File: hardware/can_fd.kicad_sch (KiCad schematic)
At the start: 11 parts

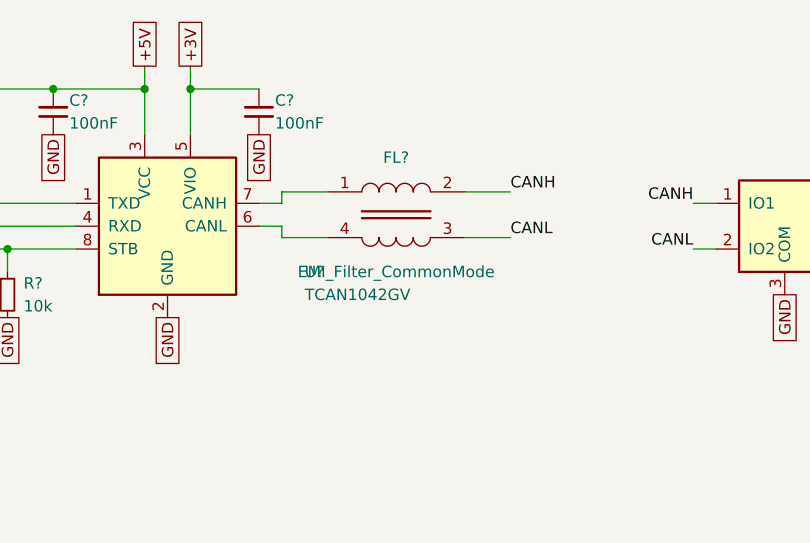
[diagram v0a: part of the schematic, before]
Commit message: Add sensing sheet; update MCU, CAN FD, encoder and root schematics
Co-Authored-By: Claude Opus 5.5 <noreply@anthropic.com>
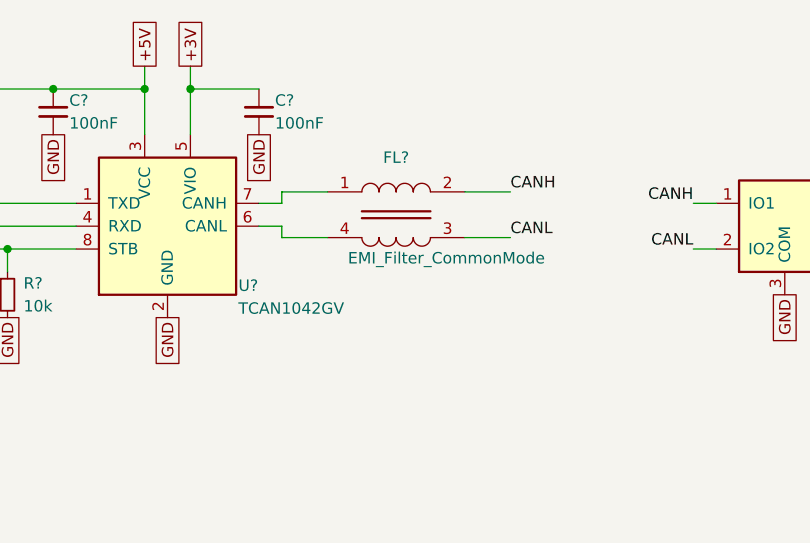
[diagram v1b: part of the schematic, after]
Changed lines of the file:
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@@
 		)
 		(property "Value" "EMI_Filter_CommonMode"
-			(at 127 106.68 0)
+			(at 132.588 105.156 0)
 			(show_name no)
 			(do_not_autoplace no)
@@
 		(dnp no)
 		(property "Reference" "U?"
-			(at 116.84 106.68 0)
+			(at 109.474 108.204 0)
 			(show_name no)
 			(do_not_autoplace no)
@@
 		)
 		(property "Value" "TCAN1042GV"
-			(at 116.84 109.22 0)
-			(show_name no)
-			(do_not_autoplace no)
+			(at 109.474 110.744 0)
+			(show_name no)
+			(do_not_autoplace no)

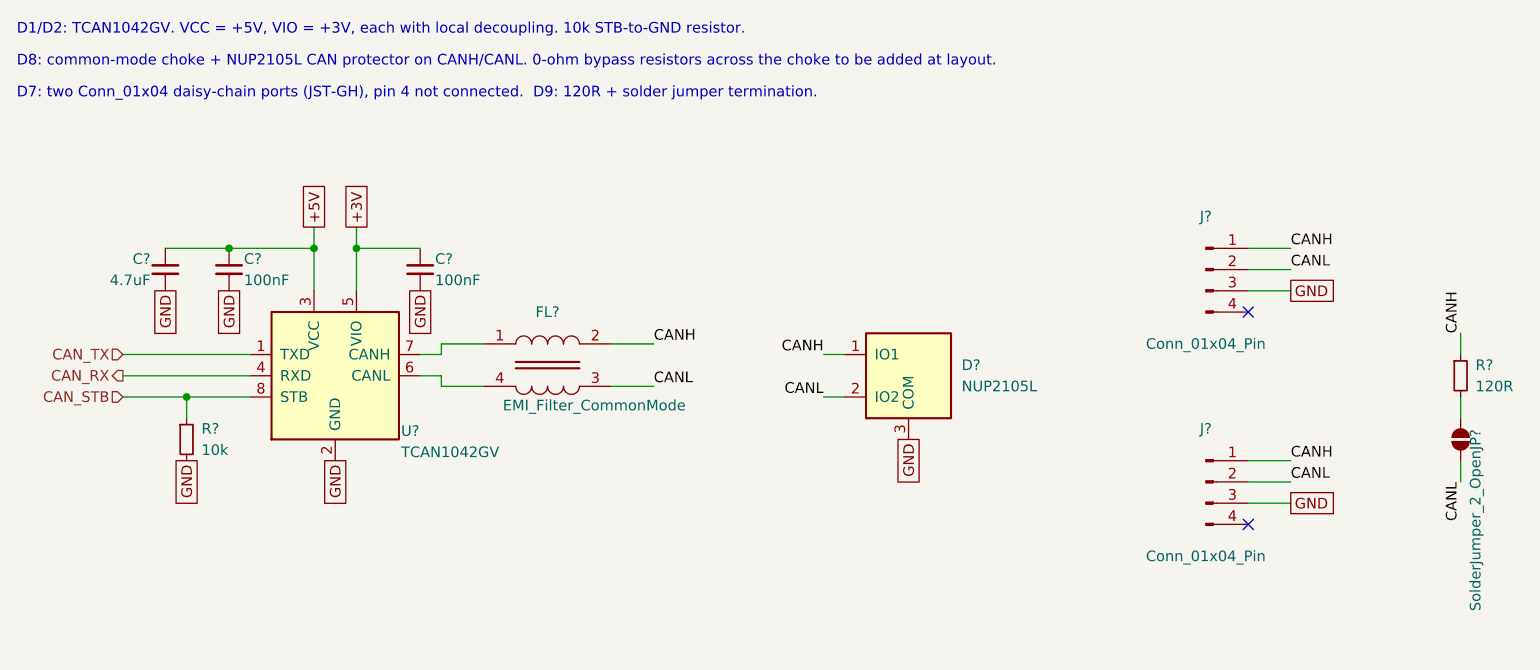
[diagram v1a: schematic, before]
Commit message: Clean up schematic ERC; add project symbol library; update README
Fix dangling labels, floating pins and pin types across the sheets so
ERC reports 0 errors (see hardware/CHANGES.txt). Add PWR_FLAGs and move
TCAN1042GV, MA702GQ and the EMI filter to nexus_drive.kicad_sym.

Update the README layout, specs and schematic review status.

Co-Authored-By: Claude Opus 5.5 <noreply@anthropic.com>
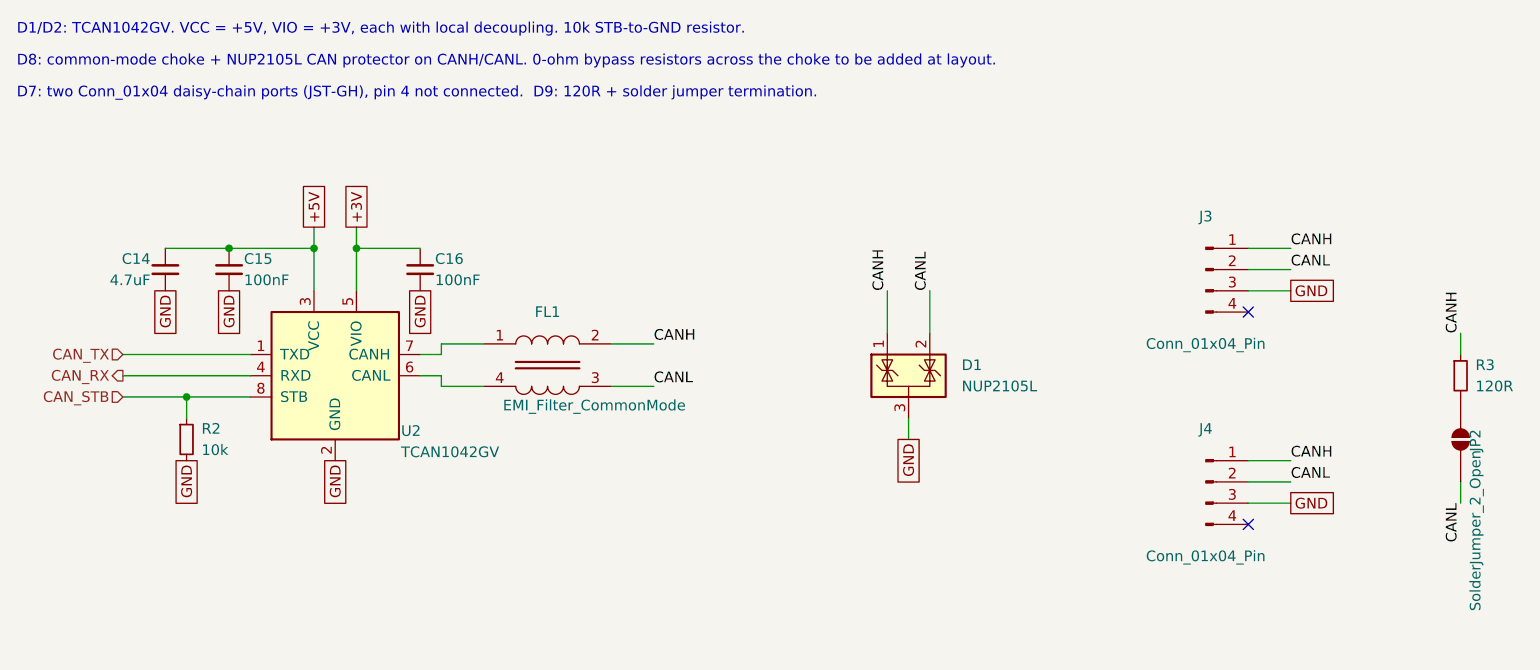
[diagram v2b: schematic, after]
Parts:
- D1: renamed from D?; footprint (none) -> Package_TO_SOT_SMD:SOT-23
- FL1: renamed from FL?; symbol Filter:EMI_Filter_CommonMode -> nexus_drive:EMI_Filter_CommonMode
- U2: renamed from U?; symbol Interface_CAN_LIN:TCAN1042GV -> nexus_drive:TCAN1042GV
- gave numbers to parts that had none: 8
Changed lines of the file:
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@@
-	(wire
-		(pts
-			(xy 162.56 104.14) (xy 160.02 104.14)
-		)
-		(stroke
-			(width 0)
-			(type default)
-		)
-	)
 	(wire
 		(pts
@@
 	(wire
 		(pts
-			(xy 162.56 99.06) (xy 160.02 99.06)
-		)
-		(stroke
-			(width 0)
-			(type default)
-		)
-	)
-	(wire
-		(pts
 			(xy 104.14 91.44) (xy 104.14 86.36)
 		)
@@
 	(wire
 		(pts
+			(xy 172.72 96.52) (xy 172.72 91.44)
+		)
+		(stroke
+			(width 0)
+			(type default)
+		)
+	)
+	(wire
+		(pts
 			(xy 83.82 104.14) (xy 91.44 104.14)
 		)
@@
 	(wire
 		(pts
-			(xy 236.22 104.14) (xy 236.22 106.68)
-		)
-		(stroke
-			(width 0)
-			(type default)
-		)
-	)
-	(wire
-		(pts
 			(xy 99.06 86.36) (xy 88.9 86.36)
 		)
@@
 	(wire
 		(pts
+			(xy 170.18 106.68) (xy 170.18 109.22)
+		)
+		(stroke
+			(width 0)
+			(type default)
+		)
+	)
+	(wire
+		(pts
 			(xy 210.82 86.36) (xy 215.9 86.36)
 		)
@@
 	(wire
 		(pts
+			(xy 167.64 96.52) (xy 167.64 91.44)
+		)
+		(stroke
+			(width 0)
+			(type default)
+		)
+	)
+	(wire
+		(pts
 			(xy 114.3 102.87) (xy 119.38 102.87)
 		)
@@
 	(wire
 		(pts
-			(xy 236.22 111.76) (xy 236.22 114.3)
+			(xy 236.22 114.3) (xy 236.22 116.84)
 		)
 		(stroke
@@
 	)
 	(label "CANH"
+		(at 167.64 91.44 90)
+		(effects
+			(font
+				(size 1.27 1.27)
+			)
+			(justify left bottom)
+		)
+	)
+	(label "CANH"
 		(at 215.9 86.36 0)
 		(effects
@@
 		)
 	)
-	(label "CANL"
-		(at 160.02 104.14 180)
-		(effects
-			(font
-				(size 1.27 1.27)
-			)
-			(justify right bottom)
-		)
-	)
 	(label "CANH"
 		(at 215.9 111.76 0)
@@
 		)
 	)
-	(label "CANH"
-		(at 160.02 99.06 180)
-		(effects
-			(font
-				(size 1.27 1.27)
-			)
-			(justify right bottom)
+	(label "CANL"
+		(at 172.72 91.44 90)
+		(effects
+			(font
+				(size 1.27 1.27)
+			)
+			(justify left bottom)
 		)
 	)
@@
 	)
 	(label "CANL"
-		(at 236.22 114.3 270)
+		(at 236.22 116.84 270)
 		(effects
 			(font
@@
 		(in_pos_files yes)
 		(dnp no)
-		(property "Reference" "JP?"
+		(property "Reference" "JP2"
 			(at 238 108 0)
 			(show_name no)
@@
 			)
 		)
-		(property "Description" ""
+		(property "Description" "Solder Jumper, 2-pole, open"
 			(at 236.22 109.22 0)
 			(hide yes)
@@
 			(project "nexus_drive"
 				(path "/2d97709d-a8ce-4889-9b37-2fa808653238/714a2a35-de05-4203-8006-3ac6d772675c"
-					(reference "JP?")
+					(reference "JP2")
 					(unit 1)
 				)
@@
 		(in_pos_files yes)
 		(dnp no)
-		(property "Reference" "R?"
+		(property "Reference" "R3"
 			(at 237.998 100.33 0)
 			(show_name no)
@@
 			)
 		)
-		(property "Description" ""
+		(property "Description" "Resistor, small symbol"
 			(at 236.22 101.6 0)
 			(hide yes)
@@
 			(project "nexus_drive"
 				(path "/2d97709d-a8ce-4889-9b37-2fa808653238/714a2a35-de05-4203-8006-3ac6d772675c"
-					(reference "R?")
+					(reference "R3")
 					(unit 1)
 				)
@@
 		(in_pos_files yes)
 		(dnp no)
-		(property "Reference" "C?"
+		(property "Reference" "C14"
 			(at 79.502 87.63 0)
 			(show_name no)
@@
 			)
 		)
-		(property "Description" ""
+		(property "Description" "Unpolarized capacitor, small symbol"
 			(at 81.28 88.9 0)
 			(hide yes)
@@
 			(project "nexus_drive"
 				(path "/2d97709d-a8ce-4889-9b37-2fa808653238/714a2a35-de05-4203-8006-3ac6d772675c"
-					(reference "C?")
+					(reference "C14")
 					(unit 1)
 				)
@@
 		(in_pos_files yes)
 		(dnp no)
-		(property "Reference" "R?"
+		(property "Reference" "R2"
 			(at 85.598 107.95 0)
 			(show_name no)
@@
 			)
 		)
-		(property "Description" ""
+		(property "Description" "Resistor, small symbol"
 			(at 83.82 109.22 0)
 			(hide yes)
@@
 			(project "nexus_drive"
 				(path "/2d97709d-a8ce-4889-9b37-2fa808653238/714a2a35-de05-4203-8006-3ac6d772675c"
-					(reference "R?")
+					(reference "R2")
 					(unit 1)
 				)
@@
 	)
 	(symbol
-		(lib_id "Filter:EMI_Filter_CommonMode")
+		(lib_id "nexus_drive:EMI_Filter_CommonMode")
 		(at 127 100.33 0)
 		(unit 1)
@@
 		(in_pos_files yes)
 		(dnp no)
-		(property "Reference" "FL?"
+		(property "Reference" "FL1"
 			(at 127 93.98 0)
 			(show_name no)
@@
 			(project "nexus_drive"
 				(path "/2d97709d-a8ce-4889-9b37-2fa808653238/714a2a35-de05-4203-8006-3ac6d772675c"
-					(reference "FL?")
+					(reference "FL1")
 					(unit 1)
 				)
@@
 		(in_pos_files yes)
 		(dnp no)
-		(property "Reference" "D?"
+		(property "Reference" "D1"
 			(at 176.53 100.33 0)
 			(show_name no)
@@
 			)
 		)
-		(property "Footprint" ""
+		(property "Footprint" "Package_TO_SOT_SMD:SOT-23"
 			(at 170.18 101.6 0)
 			(hide yes)
@@
 			)
 		)
-		(property "Datasheet" "~"
+		(property "Datasheet" "https://www.onsemi.com/pub_link/Collateral/NUP2105L-D.PDF"
 			(at 170.18 101.6 0)
 			(hide yes)
@@
 			)
 		)
-		(property "Description" ""
+		(property "Description" "Dual Line CAN Bus Protector, 24Vrwm"
 			(at 170.18 101.6 0)
 			(hide yes)
@@
 			(project "nexus_drive"
 				(path "/2d97709d-a8ce-4889-9b37-2fa808653238/714a2a35-de05-4203-8006-3ac6d772675c"
-					(reference "D?")
+					(reference "D1")
 					(unit 1)
 				)
@@
 		(in_pos_files yes)
 		(dnp no)
-		(property "Reference" "J?"
+		(property "Reference" "J3"
 			(at 205.74 82.55 0)
 			(show_name no)
@@
 			)
 		)
-		(property "Description" ""
+		(property "Description" "Generic connector, single row, 01x04, script generated"
 			(at 205.74 88.9 0)
 			(hide yes)
@@
 			(project "nexus_drive"
 				(path "/2d97709d-a8ce-4889-9b37-2fa808653238/714a2a35-de05-4203-8006-3ac6d772675c"
-					(reference "J?")
+					(reference "J3")
 					(unit 1)
 				)
@@
 		(in_pos_files yes)
 		(dnp no)
-		(property "Reference" "C?"
+		(property "Reference" "C15"
 			(at 90.678 87.63 0)
 			(show_name no)
@@
 			)
 		)
-		(property "Description" ""
+		(property "Description" "Unpolarized capacitor, small symbol"
 			(at 88.9 88.9 0)
 			(hide yes)
@@
 			(project "nexus_drive"
 				(path "/2d97709d-a8ce-4889-9b37-2fa808653238/714a2a35-de05-4203-8006-3ac6d772675c"
-					(reference "C?")
+					(reference "C15")
 					(unit 1)
 				)
@@
 		(in_pos_files yes)
 		(dnp no)
-		(property "Reference" "C?"
+		(property "Reference" "C16"
 			(at 113.538 87.63 0)
 			(show_name no)
@@
 			)
 		)
-		(property "Description" ""
+		(property "Description" "Unpolarized capacitor, small symbol"
 			(at 111.76 88.9 0)
 			(hide yes)
@@
 			(project "nexus_drive"
 				(path "/2d97709d-a8ce-4889-9b37-2fa808653238/714a2a35-de05-4203-8006-3ac6d772675c"
-					(reference "C?")
+					(reference "C16")
 					(unit 1)
 				)
@@
 		(in_pos_files yes)
 		(dnp no)
-		(property "Reference" "J?"
+		(property "Reference" "J4"
 			(at 205.74 107.95 0)
 			(show_name no)
@@
 			)
 		)
-		(property "Description" ""
+		(property "Description" "Generic connector, single row, 01x04, script generated"
 			(at 205.74 114.3 0)
 			(hide yes)
@@
 			(project "nexus_drive"
 				(path "/2d97709d-a8ce-4889-9b37-2fa808653238/714a2a35-de05-4203-8006-3ac6d772675c"
-					(reference "J?")
+					(reference "J4")
 					(unit 1)
 				)
@@
 	)
 	(symbol
-		(lib_id "Interface_CAN_LIN:TCAN1042GV")
+		(lib_id "nexus_drive:TCAN1042GV")
 		(at 101.6 101.6 0)
 		(unit 1)
@@
 		(in_pos_files yes)
 		(dnp no)
-		(property "Reference" "U?"
+		(property "Reference" "U2"
 			(at 109.474 108.204 0)
 			(show_name no)
@@
 			(project "nexus_drive"
 				(path "/2d97709d-a8ce-4889-9b37-2fa808653238/714a2a35-de05-4203-8006-3ac6d772675c"
-					(reference "U?")
+					(reference "U2")
 					(unit 1)
 				)
